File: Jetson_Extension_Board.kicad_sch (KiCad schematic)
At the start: 13 parts, among them J14 Conn_01x06_Pin, J15 Conn_01x04_Pin, J16 Pot1, J17 Pot2, J18 Pots_to_Nucleo, J6 40_Pin_Jetson_Connector, SW1 SW_Push_DPDT

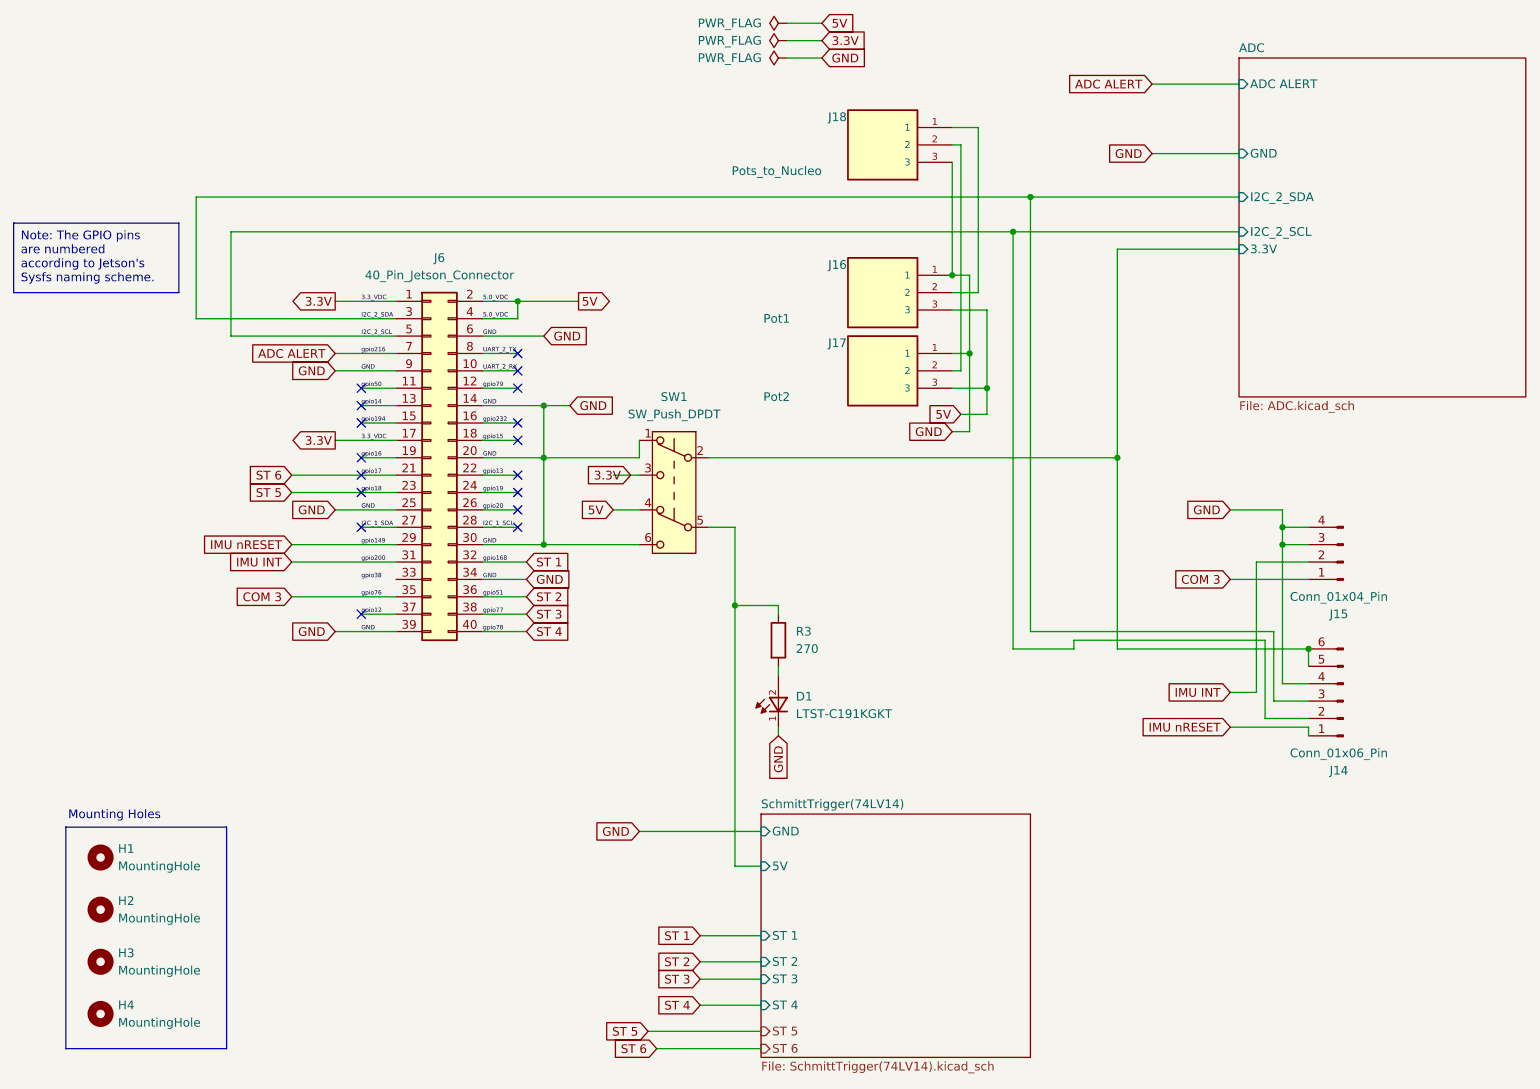
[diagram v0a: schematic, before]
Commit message: added i2c bus pins, fixed errors, is ready for a final review
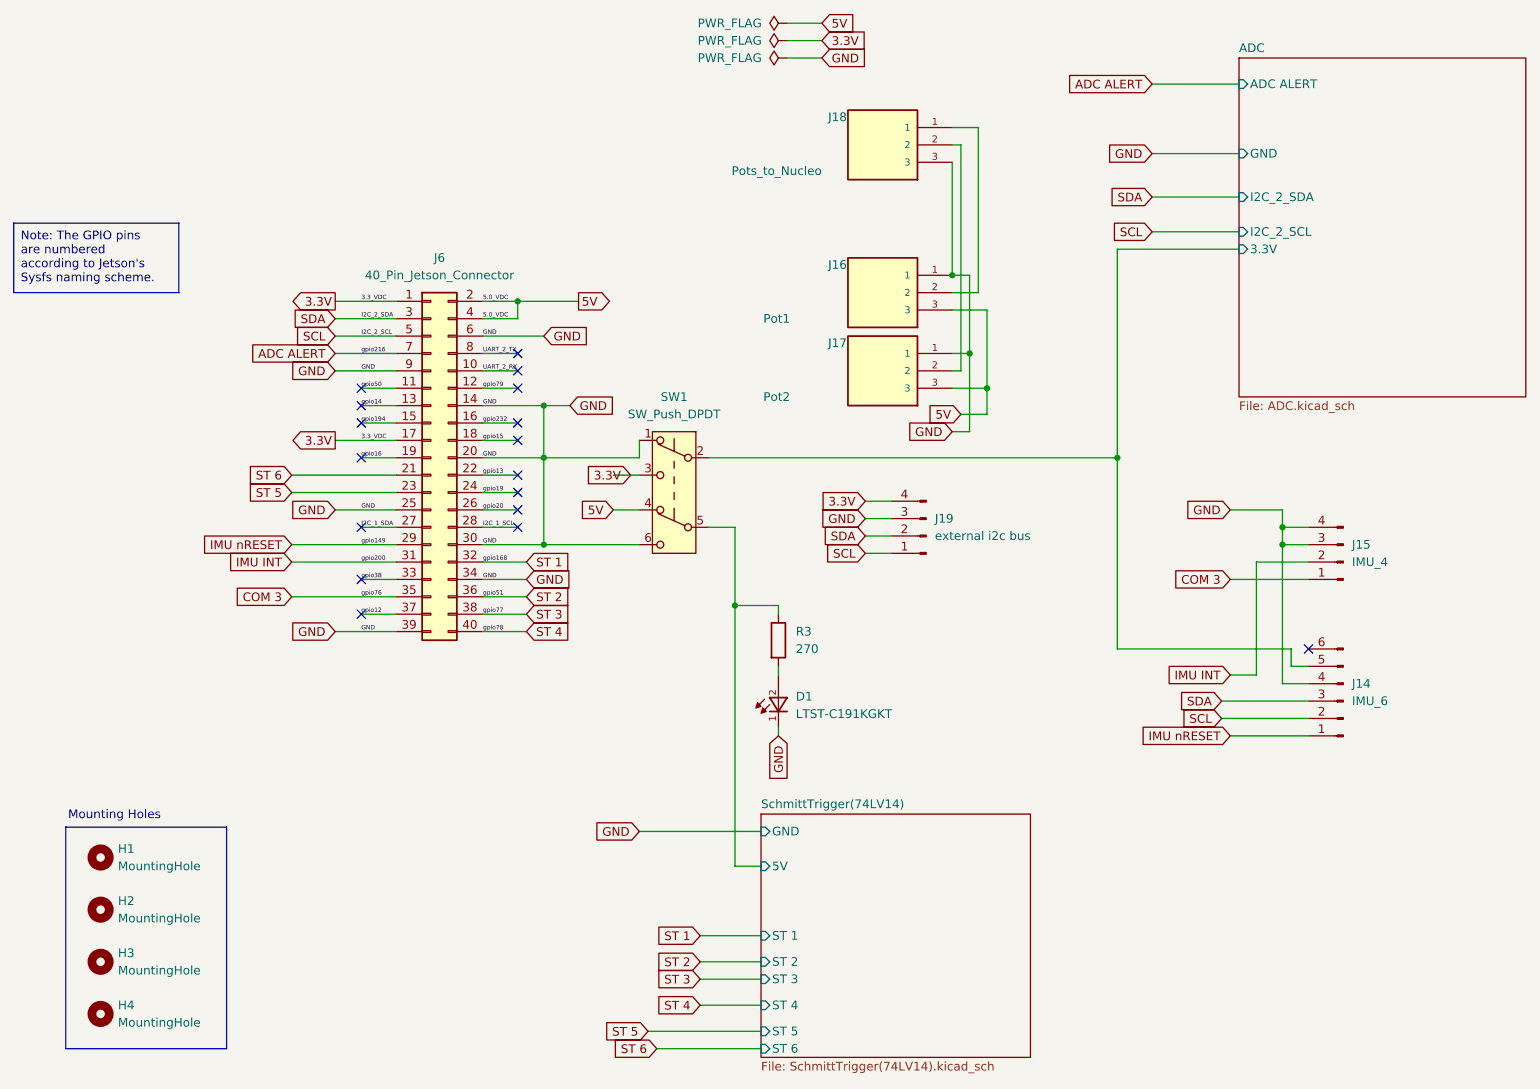
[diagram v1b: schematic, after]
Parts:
- added J19: external i2c bus, Connector_PinSocket_2.54mm:PinSocket_1x04_P2.54mm_Vertical, symbol Connector:Conn_01x04_Pin
- J14: value Conn_01x06_Pin -> IMU_6
- J15: value Conn_01x04_Pin -> IMU_4
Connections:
- net 3.3V: now also J19.4 (Pin_4)
- net ADC/3.3V: no longer J14.6 (Pin_6)
- net GND: now also J19.3 (Pin_3)
- net gpio38: now also J6.33 (Pin_33)
- net I2C_2_SCL renamed SCL
- net SCL: now also J19.1 (Pin_1)
- net I2C_2_SDA renamed SDA
- net SDA: now also J19.2 (Pin_2)
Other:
- sheet SchmittTrigger(74LV14) ports: added ST 5, ST 6; removed none

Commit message: made more fixes to JEB
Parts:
- D1: footprint LTST_C191KGKT:0603 -> LTST-C191KGKT:0603
- J19: footprint Connector_PinSocket_2.54mm:PinSocket_1x04_P2.54mm_Vertical -> TerminalBlock:TBP04R2-500-04BE
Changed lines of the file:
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@@
 			)
 		)
-		(property "Footprint" "Connector_PinSocket_2.54mm:PinSocket_1x04_P2.54mm_Vertical"
+		(property "Footprint" "TerminalBlock:TBP04R2-500-04BE"
 			(at 149.86 107.95 0)
 			(effects
@@
 			)
 		)
-		(property "Footprint" "LTST_C191KGKT:0603"
+		(property "Footprint" "LTST-C191KGKT:0603"
 			(at 128.27 133.35 0)
 			(effects

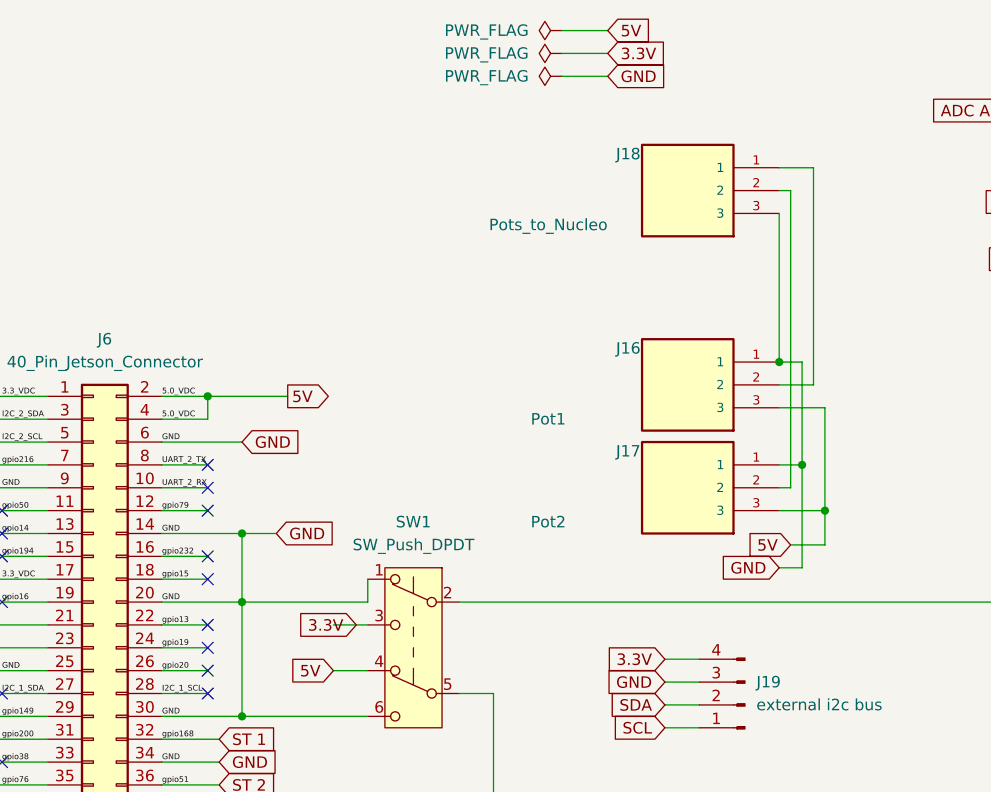
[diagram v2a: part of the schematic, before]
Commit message: replaced pot blocks with a nucleo reset block
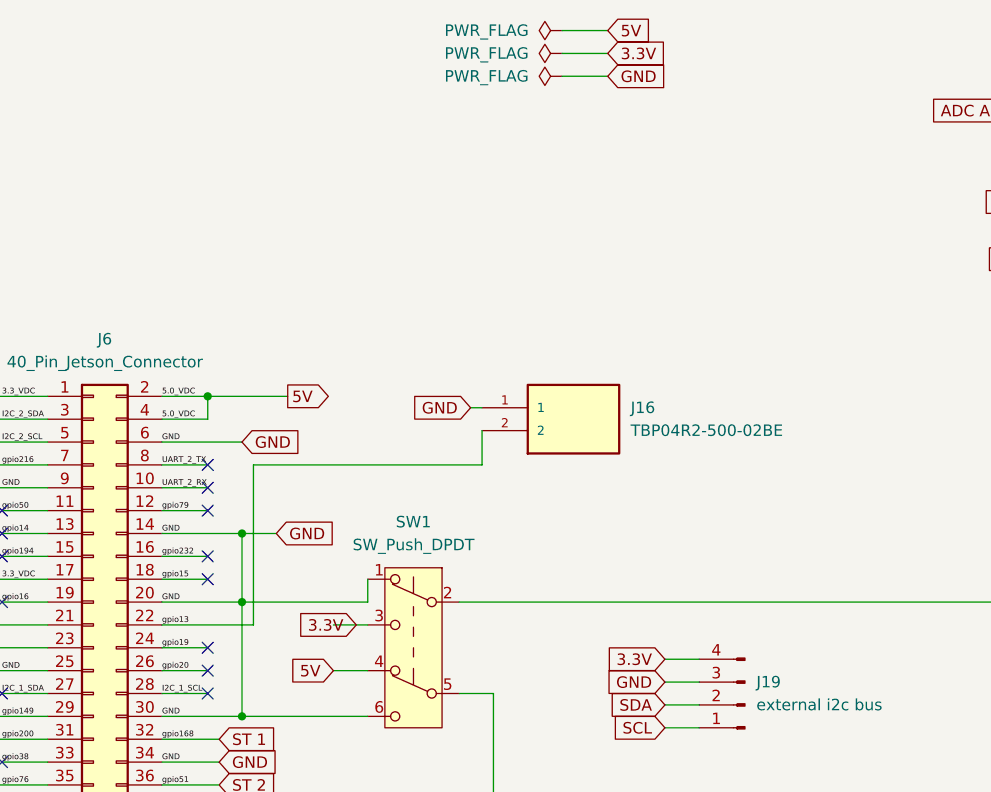
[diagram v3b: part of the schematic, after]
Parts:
- removed J16: Pot1, TBP03R2_350_03BE(1):CUI_TBP03R2-350-03BE, symbol TBP03R2-350-03BE:TBP03R2-350-03BE
- removed J17: Pot2, TBP03R2_350_03BE(1):CUI_TBP03R2-350-03BE, symbol TBP03R2-350-03BE:TBP03R2-350-03BE
- removed J18: Pots_to_Nucleo, TBP03R2_350_03BE(1):CUI_TBP03R2-350-03BE, symbol TBP03R2-350-03BE:TBP03R2-350-03BE
- added J16: TBP04R2-500-02BE, TerminalBlock:CUI_TBP04R2-500-02BE, symbol TBP04R2-500-02BE:TBP04R2-500-02BE
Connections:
- net GND: now also J16.1
- net gpio13: now also J16.2
- no-connect marks 17 -> 16
